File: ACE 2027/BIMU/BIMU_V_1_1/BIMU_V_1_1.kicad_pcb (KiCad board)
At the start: 4 copper layers, 40 x 35 mm, 53 parts, among them J201 UART_connector, J202 USB_C_Receptacle_USB2.0_16P, J203 RJ45, J204 RJ45, SW201 SW_Push, SW202 SW_Push, U101 AP7361C-33E, U201 ESP32-C3, U202 SN65HVD232DR, U301 LSM6DSV16BXTR, Y201 ABM8-40.000MHZ-10-D1G-T

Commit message: Fixer le PCB
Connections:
- U201 pad 11: unconnected-(U201-VDD3P3_RTC-Pad11) -> +3.3V
- U201 pad 17: unconnected-(U201-VDD3P3_CPU-Pad17) -> +3.3V
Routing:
- net +3.3V: track 38.4 -> 44.0 mm, vias 27 -> 29

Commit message: Update le silkscreen
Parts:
- renumbered TP103 to 3.3V, TP102 to 5V, SW202 to BOOT, TP201 to CAN+, TP202 to CAN-, D202 to CONNECTED, SW201 to EN, D203 to ERROR, TP101 to GND, D101 to POWER
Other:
- board text added: "BIMU V1.1"
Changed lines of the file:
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@@
 		(descr "Ultra-small-sized Tactile Switch with High Contact Reliability, Top-actuated Model, without Ground Terminal, without Boss")
 		(tags "Tactile Switch")
-		(property "Reference" "SW202"
+		(property "Reference" "BOOT"
 			(at 0 -2.5 90)
 			(layer "F.SilkS")
@@
 		(descr "LED SMD 0805 (2012 Metric), square (rectangular) end terminal, IPC-7351 nominal, (Body size source: https://docs.google.com/spreadsheets/d/1BsfQQcO9C6DZCsRaXUlFlo91Tg2WpOkGARC1WS5S8t0/edit?usp=sharing), generated with kicad-footprint-generator")
 		(tags "LED handsolder")
-		(property "Reference" "D202"
+		(property "Reference" "CONNECTED"
 			(at -0.127501 1.794999 0)
 			(layer "F.SilkS")
@@
 		(descr "LED SMD 0805 (2012 Metric), square (rectangular) end terminal, IPC-7351 nominal, (Body size source: https://docs.google.com/spreadsheets/d/1BsfQQcO9C6DZCsRaXUlFlo91Tg2WpOkGARC1WS5S8t0/edit?usp=sharing), generated with kicad-footprint-generator")
 		(tags "LED handsolder")
-		(property "Reference" "D203"
+		(property "Reference" "ERROR"
 			(at -0.127501 1.789999 0)
 			(layer "F.SilkS")
@@
 		(descr "Ultra-small-sized Tactile Switch with High Contact Reliability, Top-actuated Model, without Ground Terminal, without Boss")
 		(tags "Tactile Switch")
-		(property "Reference" "SW201"
+		(property "Reference" "EN"
 			(at 0 -2.5 90)
 			(layer "F.SilkS")
@@
 		(descr "LED SMD 0805 (2012 Metric), square (rectangular) end terminal, IPC-7351 nominal, (Body size source: https://docs.google.com/spreadsheets/d/1BsfQQcO9C6DZCsRaXUlFlo91Tg2WpOkGARC1WS5S8t0/edit?usp=sharing), generated with kicad-footprint-generator")
 		(tags "LED handsolder")
-		(property "Reference" "D101"
+		(property "Reference" "POWER"
 			(at -0.127501 1.799999 0)
 			(layer "F.SilkS")
@@
 		(descr "SMD rectangular pad as test Point, square 1.0mm side length")
 		(tags "test point SMD pad rectangle square")
-		(property "Reference" "TP201"
+		(property "Reference" "CAN+"
 			(at 0 1.448 180)
 			(layer "B.SilkS")
@@
 		(descr "SMD rectangular pad as test Point, square 1.0mm side length")
 		(tags "test point SMD pad rectangle square")
-		(property "Reference" "TP101"
+		(property "Reference" "GND"
 			(at 0 1.448 180)
 			(layer "B.SilkS")
@@
 		(descr "SMD rectangular pad as test Point, square 1.0mm side length")
 		(tags "test point SMD pad rectangle square")
-		(property "Reference" "TP202"
+		(property "Reference" "CAN-"
 			(at 0 1.448 180)
 			(layer "B.SilkS")
@@
 		(descr "SMD rectangular pad as test Point, square 1.0mm side length")
 		(tags "test point SMD pad rectangle square")
-		(property "Reference" "TP102"
+		(property "Reference" "5V"
 			(at 0 1.448 180)
 			(layer "B.SilkS")
@@
 		(descr "SMD rectangular pad as test Point, square 1.0mm side length")
 		(tags "test point SMD pad rectangle square")
-		(property "Reference" "TP103"
+		(property "Reference" "3.3V"
 			(at 0.6 1.5 180)
 			(layer "B.SilkS")
@@
 		(layer "Edge.Cuts")
 	)
+	(gr_text "BIMU V1.1"
+		(at 174.51 54.33 0)
+		(layer "F.SilkS")
+		(effects
+			(font
+				(size 0.85 0.85)
+				(thickness 0.2)
+				(bold yes)
+			)
+			(justify left bottom)
+		)
+	)
 	(gr_text "Conception: Josserand-Pierre Gay\nVérification: Samuel Savaria"

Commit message: Rajouté une switch demandé par Éloi
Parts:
- added CAN: SW_CAN, Button_Switch_SMD:SW_SPDT_CK_JS102011SAQN, B.Cu at (176.6, 82.6)
- moved GND 38.7 mm to (201.8, 55.0), turned to 180 degrees
- moved 3.3V 34.9 mm to (207.3, 78.7)
- moved C103 11.4 mm to (171.5, 73.0), turned to 90 degrees
- moved R211 5.18 mm to (189.3, 80.9)
- moved R212 5.09 mm to (187.9, 85.9)
- renumbered 5V to TP102, CAN+ to TP201, CAN- to TP202
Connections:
- R212 pad 2: CAN_N -> Net-(SW203-B)
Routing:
- net +3.3V: track 44.0 -> 58.3 mm, vias 29 -> 24
- net Net-(SW203-B): track 0.00 -> 9.29 mm
- net CAN_N: track 36.7 -> 45.8 mm
- net CAN_P: track 39.1 -> 35.1 mm
- net EN: track 32.4 -> 33.4 mm, vias 3 -> 4
- net GND: track 52.3 -> 51.7 mm, vias 49 -> 45
- net CONNECTED LED: track 36.1 -> 36.2 mm, vias 3 -> 5
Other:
- board text added: "END"

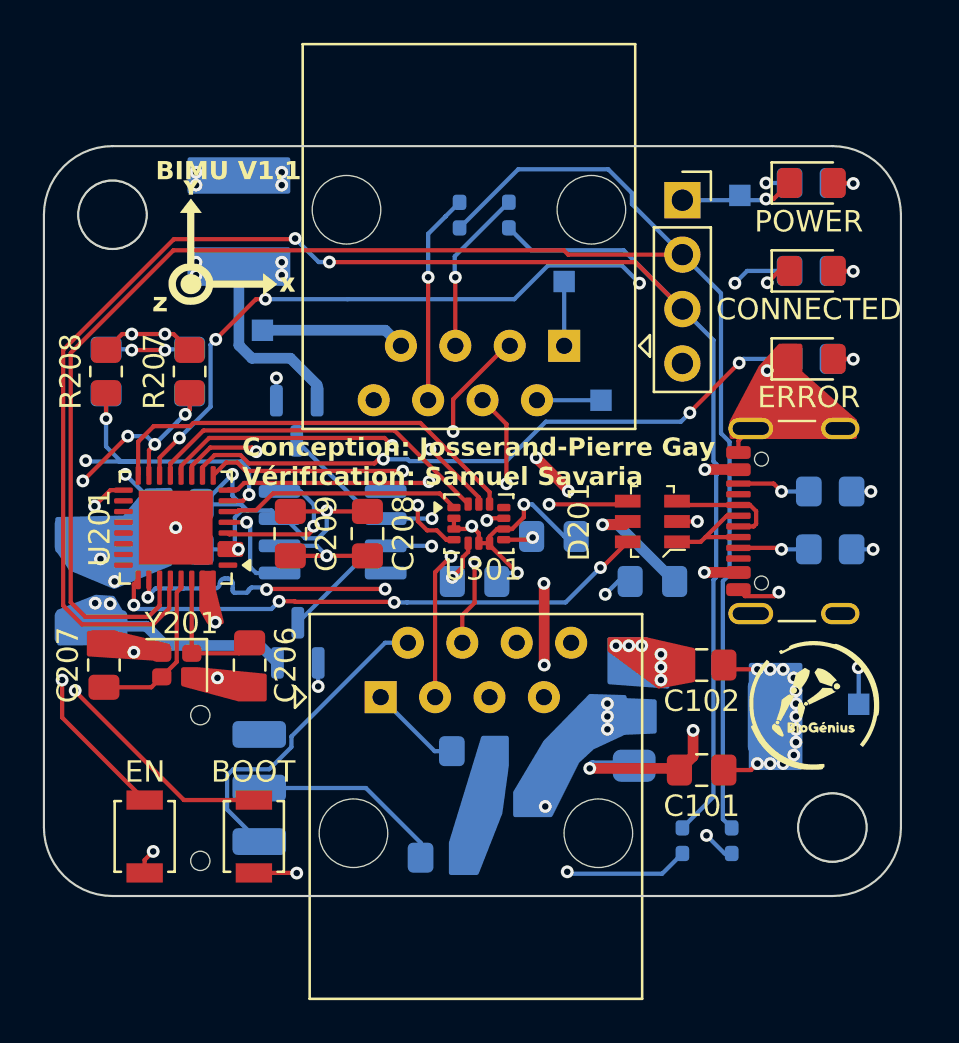
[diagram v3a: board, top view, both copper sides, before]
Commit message: Fixer les erreurs commise avec le CAN
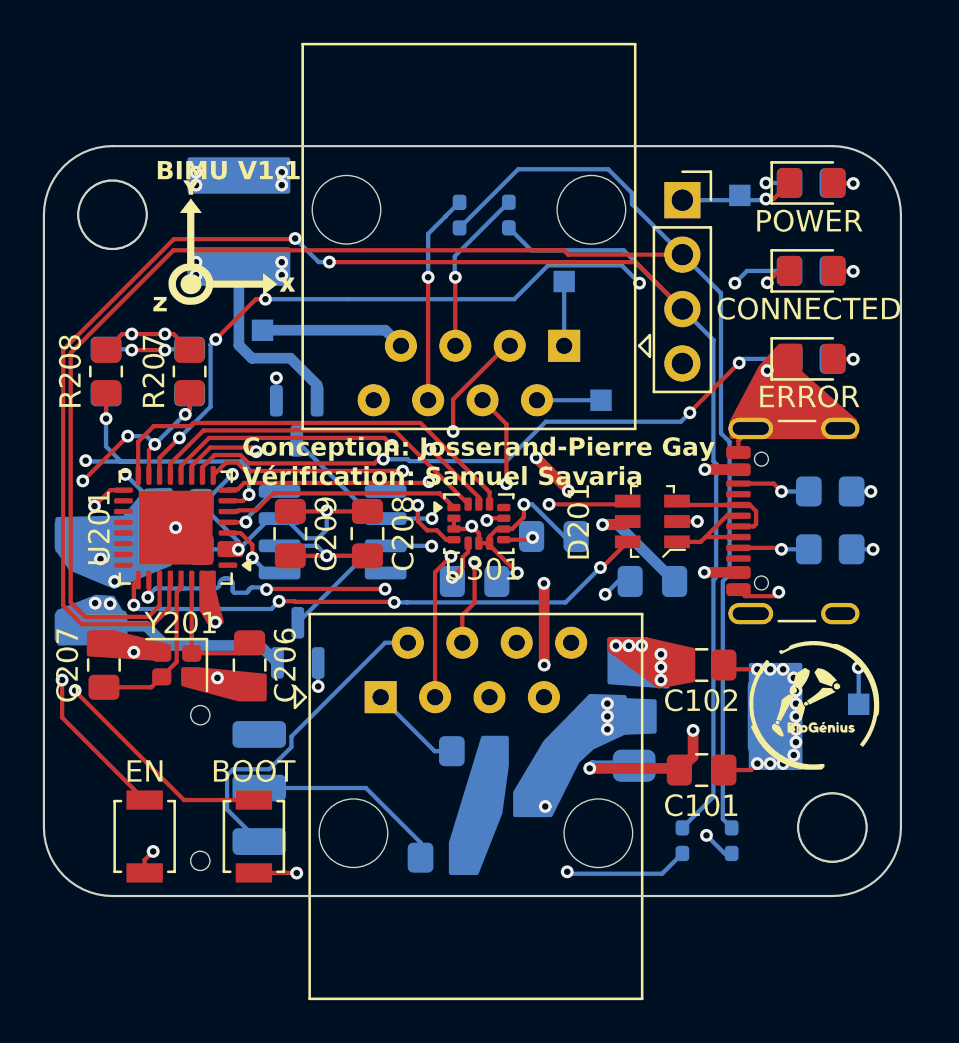
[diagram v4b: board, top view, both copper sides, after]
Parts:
- renumbered POWER to D101, CONNECTED to D202, ERROR to D203, EN to SW201, BOOT to SW202, CAN to SW203, GND to TP101, 3.3V to TP103
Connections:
- U202 pad 1: TWAI_CAN_TX -> TWAI_CAN_RX
- U202 pad 4: TWAI_CAN_RX -> TWAI_CAN_TX
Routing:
- net TWAI_CAN_RX: track 7.13 -> 3.64 mm
- net TWAI_CAN_TX: track 4.52 -> 3.09 mm
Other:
- board text added: "3.3V"
- board text added: "5V"
- board text added: "BOOT"
- board text added: "CAN"
- board text added: "CAN_N"
- board text added: "CAN_P"
- board text added: "CONNECTED"
- board text added: "EN"
- board text added: "ERROR"
- board text added: "GND"
- board text added: "POWER"

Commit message: Faire les modifications requise pour le pcb
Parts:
- added D104: D_Schottky, Diode_SMD:D_0805_2012Metric_Pad1.15x1.40mm_HandSolder, F.Cu at (200.1, 85.0)
- added D105: D_Schottky, Diode_SMD:D_0805_2012Metric_Pad1.15x1.40mm_HandSolder, F.Cu at (207.3, 77.8)
- moved TP102 22.3 mm to (201.8, 60.5)
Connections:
- J202 pad A4: +5V -> +5V_USB
- J202 pad A9: +5V -> +5V_USB
- J202 pad B4: +5V -> +5V_USB
- J202 pad B9: +5V -> +5V_USB
- J203 pad 7: +5V -> +5V_BAT
- J204 pad 7: +5V -> +5V_BAT
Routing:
- net +5V_BAT: track 0.00 -> 36.5 mm, vias 0 -> 1
- net +5V: track 73.2 -> 51.4 mm, vias 9 -> 6
- net +5V_USB: track 0.00 -> 17.3 mm
- net Net-(J204-Pad6): track 16.0 -> 17.8 mm
- net GND: track 51.7 -> 50.0 mm, vias 45 -> 46
- net +3.3V: track 58.2 -> 58.9 mm
